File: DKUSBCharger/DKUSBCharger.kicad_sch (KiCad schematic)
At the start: 4 parts, among them J1 87583-2010BLF, J2 10118192-0002LF, J3 USB4125-GF-A

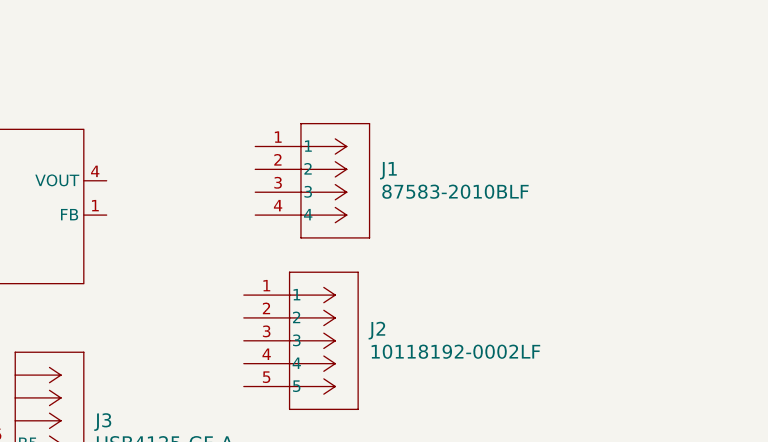
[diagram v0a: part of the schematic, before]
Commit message: added fuse and schottky diode
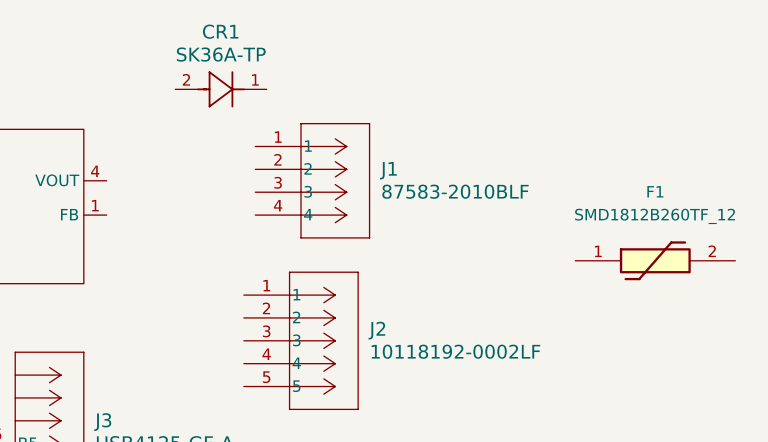
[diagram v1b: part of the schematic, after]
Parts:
- added CR1: SK36A-TP, SMCDO-214AB_MCC, symbol 2025-02-28_01-18-47:SK36A-TP
- added F1: SMD1812B260TF_12, FUSC4632X205N, symbol SMD1812B260TF_12:SMD1812B260TF_12
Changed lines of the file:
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@@
+		)
+	)
+	(symbol
+		(lib_id "SMD1812B260TF_12:SMD1812B260TF_12")
+		(at 201.93 114.3 0)
+		(unit 1)
+		(exclude_from_sim no)
+		(in_bom yes)
+		(on_board yes)
+		(dnp no)
+		(fields_autoplaced yes)
+		(property "Reference" "F1"
+			(at 210.82 106.68 0)
+			(effects
+				(font
+					(size 1.27 1.27)
+				)
+			)
+		)
+		(property "Value" "SMD1812B260TF_12"
+			(at 210.82 109.22 0)
+			(effects
+				(font
+					(size 1.27 1.27)
+				)
+			)
+		)
+		(property "Footprint" "FUSC4632X205N"
+			(at 215.9 210.49 0)
+			(effects
+				(font
+					(size 1.27 1.27)
+				)
+				(justify left top)
+				(hide yes)
+			)
+		)
+		(property "Datasheet" "https://www.yageo.com/upload/media/product/productsearch/datasheet/cpc/pptc/SMD1812_1.pdf"
+			(at 215.9 310.49 0)
+			(effects
+				(font
+					(size 1.27 1.27)
+				)
+				(justify left top)
+				(hide yes)
+			)
+		)
+		(property "Description" "Resettable Fuses - PPTC PPTC 12V 2.6A"
+			(at 201.93 114.3 0)
+			(effects
+				(font
+					(size 1.27 1.27)
+				)
+				(hide yes)
+			)
+		)
+		(property "Height" "2.05"
+			(at 215.9 510.49 0)
+			(effects
+				(font
+					(size 1.27 1.27)
+				)
+				(justify left top)
+				(hide yes)
+			)
+		)
+		(property "Manufacturer_Name" "YAGEO"
+			(at 215.9 610.49 0)
+			(effects
+				(font
+					(size 1.27 1.27)
+				)
+				(justify left top)
+				(hide yes)
+			)
+		)
+		(property "Manufacturer_Part_Number" "SMD1812B260TF/12"
+			(at 215.9 710.49 0)
+			(effects
+				(font
+					(size 1.27 1.27)
+				)
+				(justify left top)
+				(hide yes)
+			)
+		)
+		(property "Mouser Part Number" "603-SMD1812B260TF/12"
+			(at 215.9 810.49 0)
+			(effects
+				(font
+					(size 1.27 1.27)
+				)
+				(justify left top)
+				(hide yes)
+			)
+		)
+		(property "Mouser Price/Stock" "https://www.mouser.co.uk/ProductDetail/YAGEO/SMD1812B260TF-12?qs=0lSvoLzn4L8Goovhs4XJWQ%3D%3D"
+			(at 215.9 910.49 0)
+			(effects
+				(font
+					(size 1.27 1.27)
+				)
+				(justify left top)
+				(hide yes)
+			)
+		)
+		(property "Arrow Part Number" ""
+			(at 215.9 1010.49 0)
+			(effects
+				(font
+					(size 1.27 1.27)
+				)
+				(justify left top)
+				(hide yes)
+			)
+		)
+		(property "Arrow Price/Stock" ""
+			(at 215.9 1110.49 0)
+			(effects
+				(font
+					(size 1.27 1.27)
+				)
+				(justify left top)
+				(hide yes)
+			)
+		)
+		(pin "1"
+		)
+		(pin "2"
+		)
+		(instances
+			(project ""
+				(path "/78927aa5-2276-4522-b62d-c227d54319d7"
+					(reference "F1")
+					(unit 1)
+				)
+			)
+		)
+	)
+	(symbol
+		(lib_id "2025-02-28_01-18-47:SK36A-TP")
+		(at 157.48 95.25 0)
+		(unit 1)
+		(exclude_from_sim no)
+		(in_bom yes)
+		(on_board yes)
+		(dnp no)
+		(fields_autoplaced yes)
+		(property "Reference" "CR1"
+			(at 162.56 88.9 0)
+			(effects
+				(font
+					(size 1.524 1.524)
+				)
+			)
+		)
+		(property "Value" "SK36A-TP"
+			(at 162.56 91.44 0)
+			(effects
+				(font
+					(size 1.524 1.524)
+				)
+			)
+		)
+		(property "Footprint" "SMCDO-214AB_MCC"
+			(at 157.48 95.25 0)
+			(effects
+				(font
+					(size 1.27 1.27)
+					(italic yes)
+				)
+				(hide yes)
+			)
+		)
+		(property "Datasheet" "SK36A-TP"
+			(at 157.48 95.25 0)
+			(effects
+				(font
+					(size 1.27 1.27)
+					(italic yes)
+				)
+				(hide yes)
+			)
+		)
+		(property "Description" ""
+			(at 157.48 95.25 0)
+			(effects
+				(font
+					(size 1.27 1.27)
+				)
+				(hide yes)
+			)
+		)
+		(pin "1"
+		)
+		(pin "2"
+		)
+		(instances
+			(project ""
+				(path "/78927aa5-2276-4522-b62d-c227d54319d7"
+					(reference "CR1")
+					(unit 1)
+				)
+			)
 		)
 	)

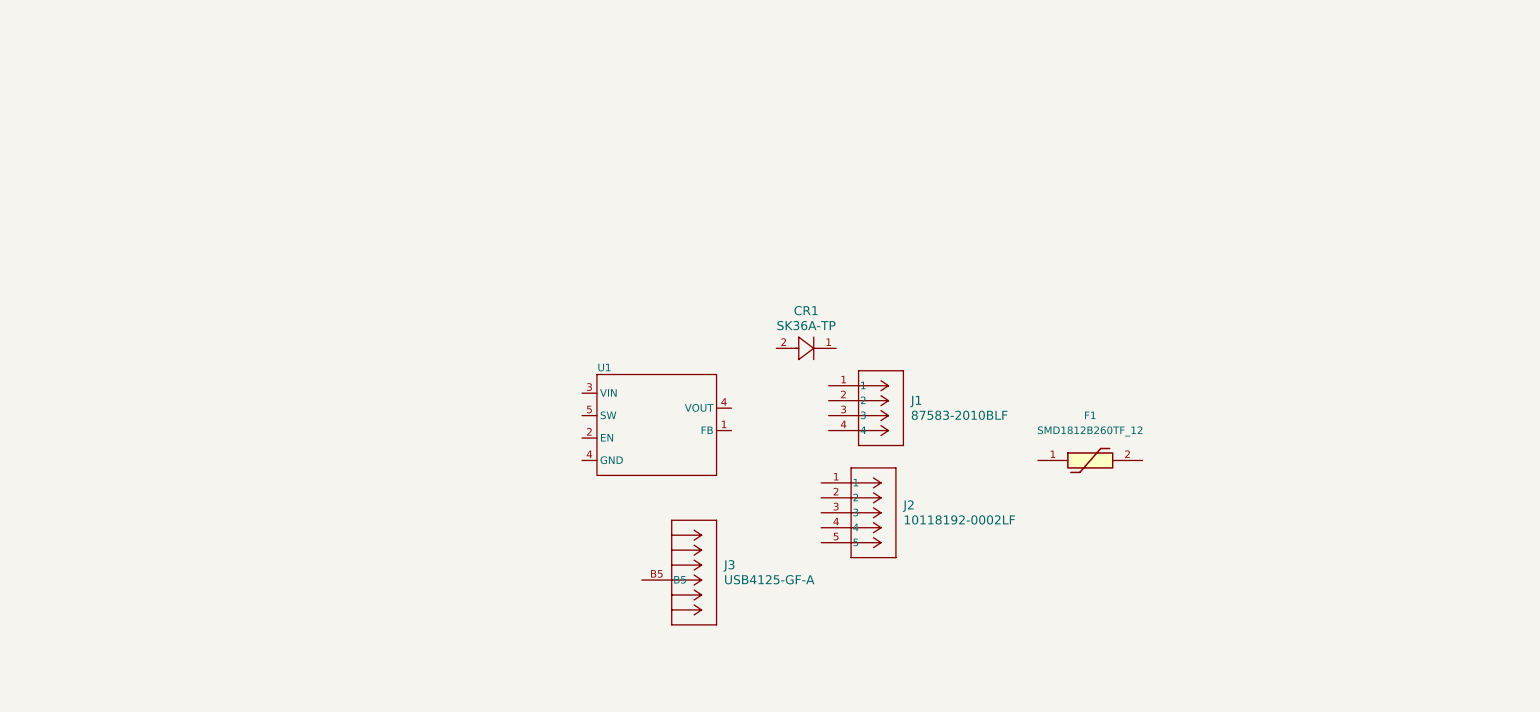
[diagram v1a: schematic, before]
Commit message: finished usb charger schematic
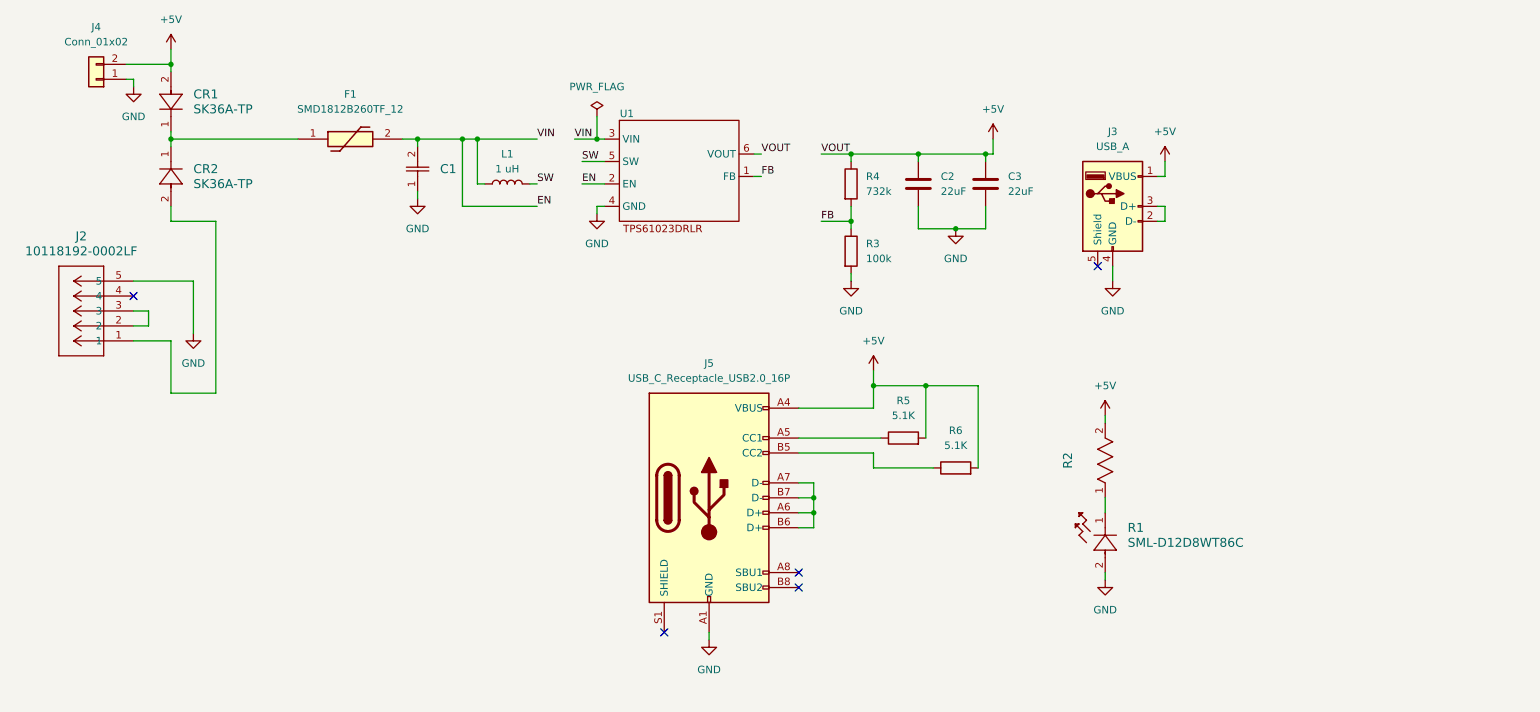
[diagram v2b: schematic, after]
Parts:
- removed J1: 87583-2010BLF, Conn_USB-87583_AMP, symbol 2025-02-28_00-42-36:87583-2010BLF
- removed J3: USB4125-GF-A, CONN6_USB4125_GCT, symbol 2025-02-28_00-47-38:USB4125-GF-A
- added C1: CL10A106KQ8NNNC, CAP_CL10_SAM, symbol 2025-02-28_03-29-39:CL10A106KQ8NNNC
- added C2, C3: 22uF, symbol Device:C
- added CR2: SK36A-TP, SMCDO-214AB_MCC, symbol 2025-02-28_01-18-47:SK36A-TP
- added J3: USB_A, symbol Connector:USB_A
- added J4: Conn_01x02, symbol Connector_Generic:Conn_01x02
- added J5: USB_C_Receptacle_USB2.0_16P, symbol Connector:USB_C_Receptacle_USB2.0_16P
- added L1: 1 uH, symbol Device:L
- added R1: SML-D12D8WT86C, LED_SMLD12_ROM, symbol 2025-02-28_03-17-54:SML-D12D8WT86C
- added R2: RR0816P-2800-D-44A, RES_0816_SUS, symbol 2025-02-28_03-24-14:RR0816P-2800-D-44A
- added R3: 100k, symbol Device:R
- added R4: 732k, symbol Device:R
- added R5, R6: 5.1K, symbol Device:R
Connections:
- net at J2.1: now also CR2.2
- net at J2.2: now also J2.3
- net GND: now reaches J2.5
- net GND: now also U1.4 (GND), C1.1, C2.2, C3.2, J3.4 (GND), J4.1 (Pin_1), J5.A1 (GND), J5.A12 (GND), J5.B1 (GND), J5.B12 (GND), R1.2, R3.2
- net FB: now reaches U1.1 (FB)
- net FB: now also R3.1, R4.2
- net EN: now reaches U1.2 (EN)
- net EN: now also F1.2, U1.3 (VIN), C1.2, L1.1
- net SW: now reaches U1.5 (SW)
- net SW: now also L1.2
- net at F1.1: now also CR1.1, CR2.1
- net +5V: now reaches CR1.2
- net +5V: now also U1.6 (VOUT), C2.1, C3.1, J3.1 (VBUS), J4.2 (Pin_2), J5.A4 (VBUS), J5.A9 (VBUS), J5.B4 (VBUS), J5.B9 (VBUS), R2.2, R4.1, R5.2, R6.2
- new net: J3.2 (D-), J3.3 (D+)
- new net: J5.A5 (CC1), R5.1
- new net: R1.1, R2.1
- new net: J5.B5 (CC2), R6.1
- new net: J5.A6 (D+), J5.A7 (D-), J5.B6 (D+), J5.B7 (D-)
- no-connect marks 0 -> 5
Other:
- moved on the sheet: CR1, F1, J2

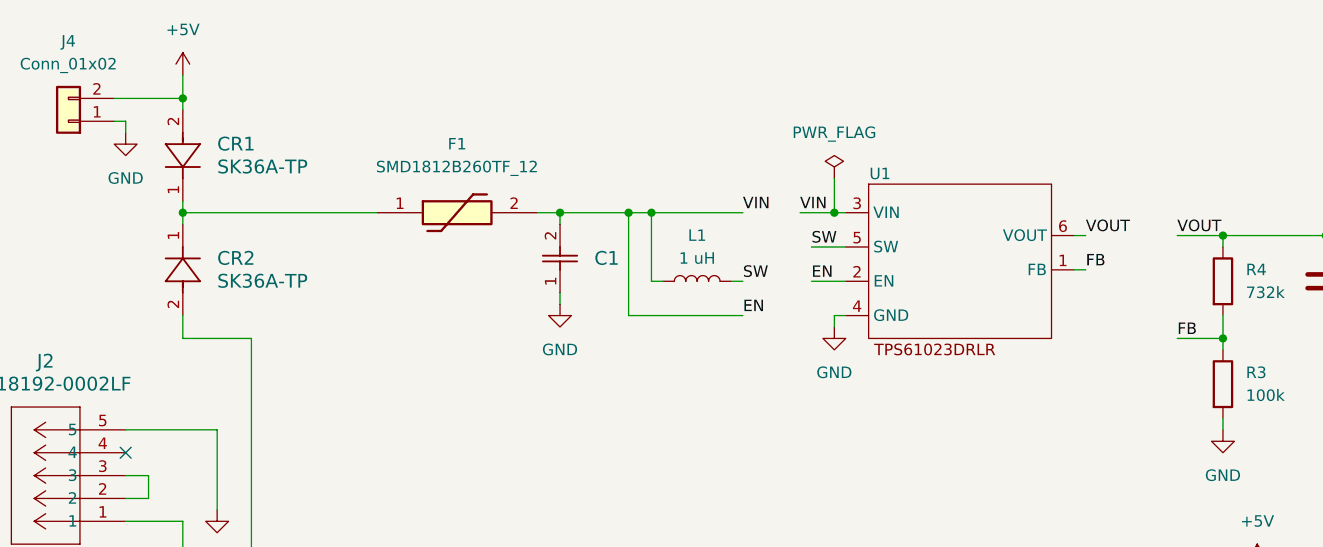
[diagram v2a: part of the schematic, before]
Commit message: Fixing schematic symbols
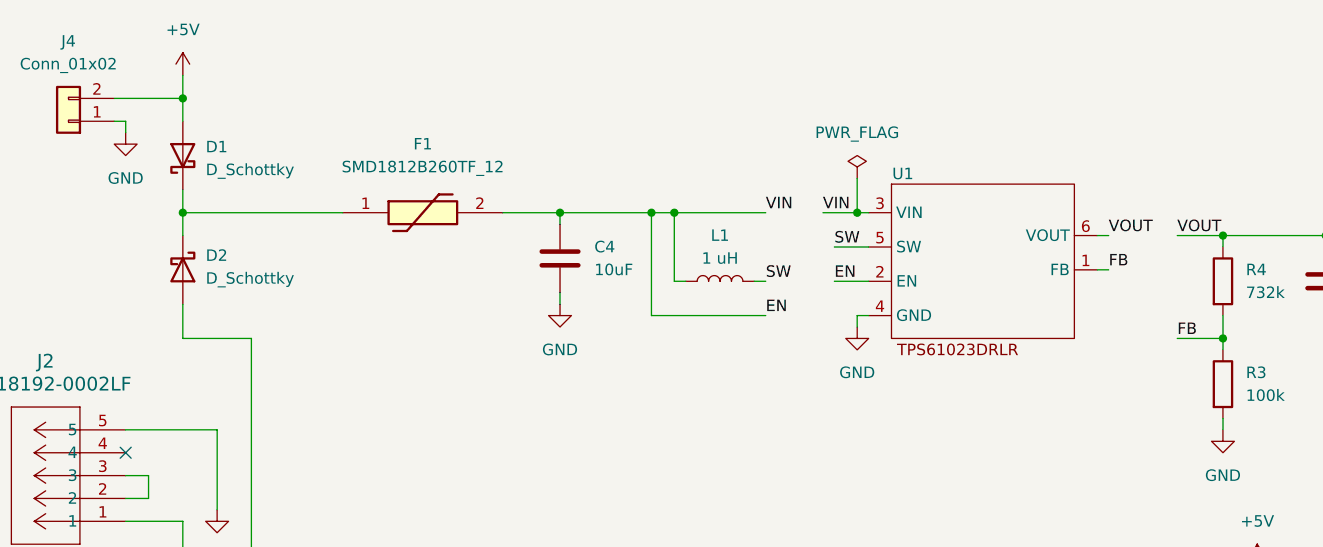
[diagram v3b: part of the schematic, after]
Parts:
- removed C1: CL10A106KQ8NNNC, CAP_CL10_SAM, symbol 2025-02-28_03-29-39:CL10A106KQ8NNNC
- removed CR1, CR2: SK36A-TP, SMCDO-214AB_MCC, symbol 2025-02-28_01-18-47:SK36A-TP
- added C4: 10uF, symbol Device:C
- added D1, D2: D_Schottky, symbol Device:D_Schottky
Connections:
- net +5V: now also D1.2 (A)
- net EN: now also C4.1
- net GND: now also C4.2
- net at J2.1: now also D2.2 (A)
- net at F1.1: now also D1.1 (K), D2.1 (K)
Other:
- moved on the sheet: F1, L1, U1

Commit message: Assigning footprints in schematic
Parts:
- removed C2, C3: 22uF, symbol Device:C
- removed C4: 10uF, symbol Device:C
- removed D1, D2: D_Schottky, symbol Device:D_Schottky
- added C1: 10uF, footprints:CAP_CL10_SAM, symbol 2025-02-28_20-33-51:CL10A106KQ8NNNC
- added C2, C3: 22uF, footprints_22uF_CAP:G-188_MUR, symbol 2025-02-28_20-38-07:GRM188R60J226MEA0D
- added CR1, CR2: SK36A-TP, SMCDO-214AB_MCC, symbol 2025-02-28_01-18-47:SK36A-TP
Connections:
- net +5V: now also C2.2, C3.2, CR1.2
- net EN: now also C1.2
- net GND: now also C1.1, C2.1, C3.1
- net at F1.1: now also CR1.1, CR2.1
- net at J2.1: now also CR2.2
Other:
- moved on the sheet: J5, R5, R6

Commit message: finished assigning footprints; updated PCB
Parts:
- removed L1: 1 uH, symbol Device:L
- removed R3: 100k, symbol Device:R
- removed R4: 732k, symbol Device:R
- removed R5, R6: 5.1K, symbol Device:R
- added L1: 1uH, Inductor_1uF:INDC2012X80N, symbol LPWI201208S1R0T:LPWI201208S1R0T
- added R1, R2: 5.1k, footprints_resistor_5.1k:RC0603N_YAG-M, symbol 2025-02-28_22-01-57:RC0603FR-075K1L
- added R3: 732k, Resistor_732k:RC0603N_PAN, symbol 2025-02-28_21-51-45:ERJ-3EKF7323V
- added R4: 100k, footprints_resistor_100k:RC0603N_PAN, symbol 2025-02-28_21-57-15:ERJ-3EKF1003V
- C1: footprint footprints:CAP_CL10_SAM -> footprints_10uF_CAP:CAP_CL10_SAM
- CR1, CR2: footprint SMCDO-214AB_MCC -> footprints_Schottky_60V_3A:SMCDO-214AB_MCC
- F1: value SMD1812B260TF_12 -> 2.6A; footprint FUSC4632X205N -> footprints_fuse_2.6A_12V:FUSC4632X205N
- J1: renamed from J4; footprint (none) -> Connector_PinHeader_2.54mm:PinHeader_1x02_P2.54mm_Vertical
- J2: footprint CONN_10118192-0002LF_AMP -> footprints_fuse_2.6A_12V:FUSC4632X205N
- J3: renamed from J5; footprint (none) -> footprints_USB_Type_C_Receptacle:CONN6_USB4125_GCT
- J4: renamed from J3; footprint (none) -> footprints_USB_Type_A_Receptacle:Conn_USB-87583_AMP
- R5: renamed from R2; value RR0816P-2800-D-44A -> 280; footprint RES_0816_SUS -> RR0816P_2800_D_44A:RESC1608X50N
- R6: renamed from R1; footprint LED_SMLD12_ROM -> footprints_LED_orange:LED_SMLD12_ROM
- U1: footprint (none) -> footprints_regulator_boost_3A_ADJ:DRL0006A
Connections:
- net +5V: now also R1.1, R2.1, R3.1
- net EN: now also L1.1
- net FB: now also R3.2, R4.1
- net GND: now also R4.2
- net SW: now also L1.2
- net CC1: now reaches J3.A5 (CC1)
- net CC1: now also R1.2
- net CC2: now reaches J3.B5 (CC2)
- net CC2: now also R2.2
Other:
- moved on the sheet: C2, C3, J3, J4, R5, R6, U1

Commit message: continuing footprint assignmnets
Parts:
- added J5: 87583-2010BLF, 875832010BLF, symbol 87583-2010BLF:87583-2010BLF
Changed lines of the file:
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@@
+	)
+	(symbol
+		(lib_id "87583-2010BLF:87583-2010BLF")
+		(at 217.17 102.87 0)
+		(unit 1)
+		(exclude_from_sim no)
+		(in_bom yes)
+		(on_board yes)
+		(dnp no)
+		(fields_autoplaced yes)
+		(property "Reference" "J5"
+			(at 228.6 95.25 0)
+			(effects
+				(font
+					(size 1.27 1.27)
+				)
+			)
+		)
+		(property "Value" "87583-2010BLF"
+			(at 228.6 97.79 0)
+			(effects
+				(font
+					(size 1.27 1.27)
+				)
+			)
+		)
+		(property "Footprint" "875832010BLF"
+			(at 236.22 197.79 0)
+			(effects
+				(font
+					(size 1.27 1.27)
+				)
+				(justify left top)
+				(hide yes)
+			)
+		)
+		(property "Datasheet" "https://cdn.amphenol-cs.com/media/wysiwyg/files/drawing/87583.pdf"
+			(at 236.22 297.79 0)
+			(effects
+				(font
+					(size 1.27 1.27)
+				)
+				(justify left top)
+				(hide yes)
+			)
+		)
+		(property "Description" "USB 2.0, Input Output Connectors, Receptacle, Type A, Standard, Right Angle, Surface Mount, Single Deck, 4 Positions"
+			(at 217.17 102.87 0)
+			(effects
+				(font
+					(size 1.27 1.27)
+				)
+				(hide yes)
+			)
+		)
+		(property "Height" "7.94"
+			(at 236.22 497.79 0)
+			(effects
+				(font
+					(size 1.27 1.27)
+				)
+				(justify left top)
+				(hide yes)
+			)
+		)
+		(property "Manufacturer_Name" "Amphenol Communications Solutions"
+			(at 236.22 597.79 0)
+			(effects
+				(font
+					(size 1.27 1.27)
+				)
+				(justify left top)
+				(hide yes)
+			)
+		)
+		(property "Manufacturer_Part_Number" "87583-2010BLF"
+			(at 236.22 697.79 0)
+			(effects
+				(font
+					(size 1.27 1.27)
+				)
+				(justify left top)
+				(hide yes)
+			)
+		)
+		(property "Mouser Part Number" ""
+			(at 236.22 797.79 0)
+			(effects
+				(font
+					(size 1.27 1.27)
+				)
+				(justify left top)
+				(hide yes)
+			)
+		)
+		(property "Mouser Price/Stock" ""
+			(at 236.22 897.79 0)
+			(effects
+				(font
+					(size 1.27 1.27)
+				)
+				(justify left top)
+				(hide yes)
+			)
+		)
+		(property "Arrow Part Number" "87583-2010BLF"
+			(at 236.22 997.79 0)
+			(effects
+				(font
+					(size 1.27 1.27)
+				)
+				(justify left top)
+				(hide yes)
+			)
+		)
+		(property "Arrow Price/Stock" "https://www.arrow.com/en/products/87583-2010blf/amphenol-fci?region=europe"
+			(at 236.22 1097.79 0)
+			(effects
+				(font
+					(size 1.27 1.27)
+				)
+				(justify left top)
+				(hide yes)
+			)
+		)
+		(pin "MH2"
+		)
+		(pin "MH1"
+		)
+		(pin "2"
+		)
+		(pin "3"
+		)
+		(pin "1"
+		)
+		(pin "4"
+		)
+		(instances
+			(project ""
+				(path "/78927aa5-2276-4522-b62d-c227d54319d7"
+					(reference "J5")
+					(unit 1)
+				)
+			)
+		)
 	)
 	(symbol

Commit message: Continuing annotations
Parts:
- removed J4: USB_A, footprints_USB_Type_A_Receptacle:Conn_USB-87583_AMP, symbol Connector:USB_A
- C1: footprint footprints_10uF_CAP:CAP_CL10_SAM -> USBChargerFootprints:CAP_CL10_SAM
- C2, C3: footprint footprints_22uF_CAP:G-188_MUR -> USBChargerFootprints:G-188_MUR
- J5: footprint 875832010BLF -> USBChargerFootprints:875832010BLF
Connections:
- net +5V: now also J5.1
- net GND: now also J5.4
- net at J5.2: now also J5.3
- no-connect marks 5 -> 6
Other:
- moved on the sheet: J5, R5, R6

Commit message: Fixed footprints
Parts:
- removed J3: USB_C_Receptacle_USB2.0_16P, footprints_USB_Type_C_Receptacle:CONN6_USB4125_GCT, symbol Connector:USB_C_Receptacle_USB2.0_16P
- added J3: USB4125-GF-A_REVA2, USBChargerFootprints:GCT_USB4125-GF-A_REVA2, symbol USBChargerSymbols:USB4125-GF-A_REVA2
- CR1, CR2: footprint footprints_Schottky_60V_3A:SMCDO-214AB_MCC -> USBChargerFootprints:SMCDO-214AB_MCC
- F1: footprint footprints_fuse_2.6A_12V:FUSC4632X205N -> USBChargerFootprints:FUSC4632X205N
- J2: footprint footprints_fuse_2.6A_12V:FUSC4632X205N -> USBChargerFootprints:CONN_10118192-0002LF_AMP
- L1: footprint Inductor_1uF:INDC2012X80N -> USBChargerFootprints:INDC2012X80N
- R1, R2: footprint footprints_resistor_5.1k:RC0603N_YAG-M -> USBChargerFootprints:RC0603N_YAG
- R3: footprint Resistor_732k:RC0603N_PAN -> USBChargerFootprints:RC0603N_PAN
- R4: footprint footprints_resistor_100k:RC0603N_PAN -> USBChargerFootprints:RC0603N_PAN_100k
- R5: footprint RR0816P_2800_D_44A:RESC1608X50N -> USBChargerFootprints:RESC1608X50N
- R6: footprint footprints_LED_orange:LED_SMLD12_ROM -> USBChargerFootprints:LED_SMLD12_ROM
- U1: footprint footprints_regulator_boost_3A_ADJ:DRL0006A -> USBChargerFootprints:DRL0006A
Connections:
- net +5V: now also R1.2, R2.2, J3.A9 (VBUS), J3.B9 (VBUS__1); no longer R1.1, R2.1
- net CC1: now also R1.1, J3.A5 (CC1); no longer R1.2
- net CC2: now also R2.1, J3.B5 (CC2); no longer R2.2
- net GND: now also J3.A12 (GND), J3.B12 (GND__1)
- no-connect marks 6 -> 7
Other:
- moved on the sheet: R1, R2
